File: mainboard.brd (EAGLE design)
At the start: 160 x 100 mm, 38 parts, among them IC1 LM358N, IC2 LM833N, IC3 74HC08N, K1 AQH213

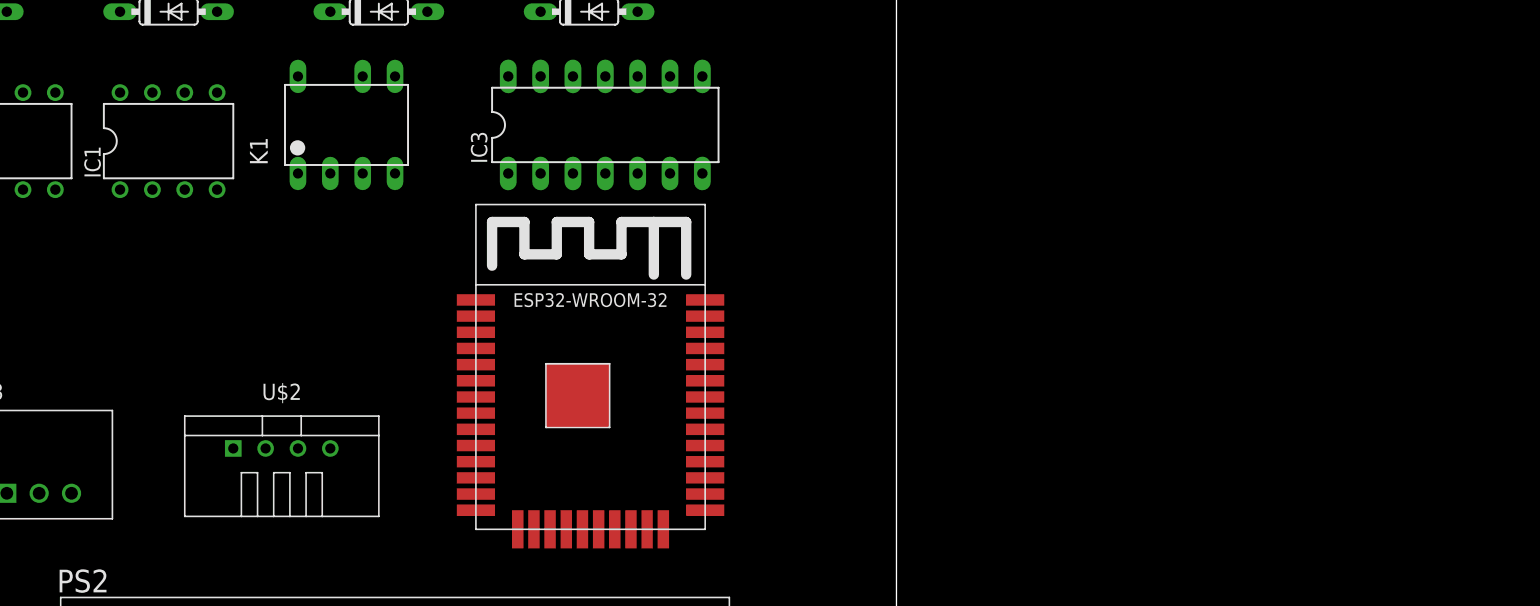
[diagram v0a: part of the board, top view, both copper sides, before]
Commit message: Added optos for sensing L and N (l1/l2)
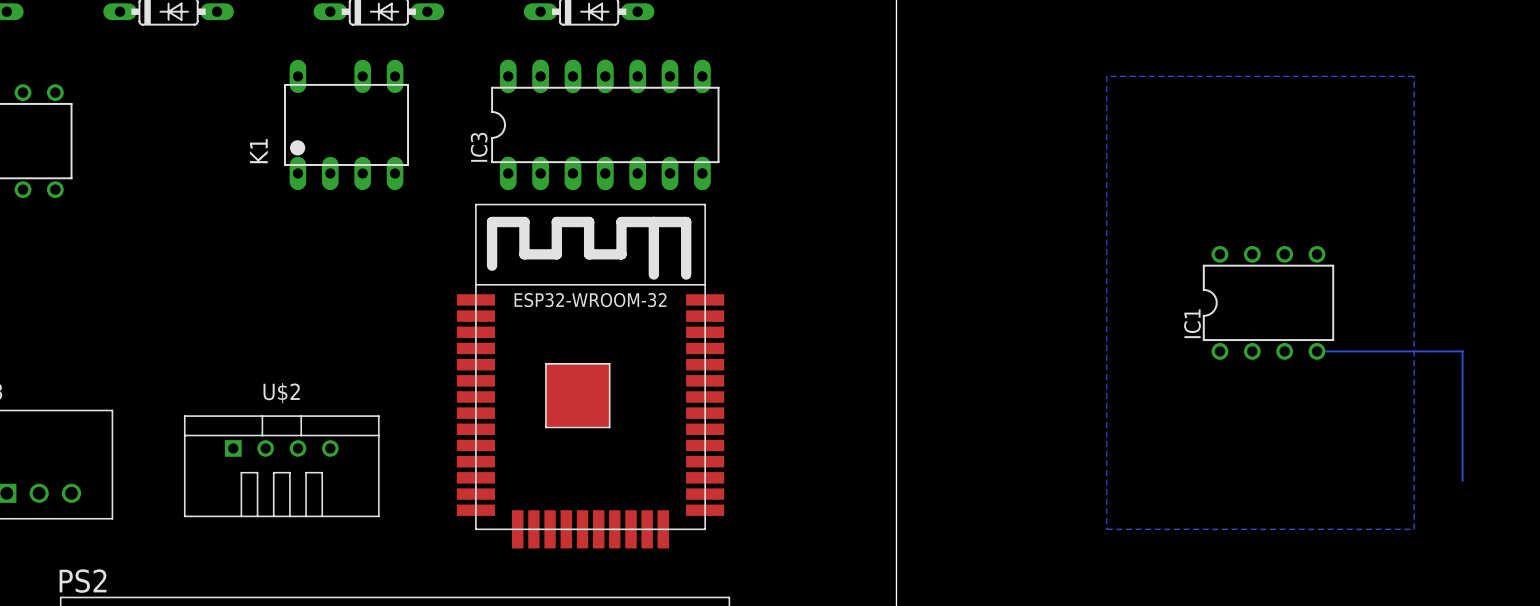
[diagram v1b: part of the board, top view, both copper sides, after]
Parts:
- moved IC1 87.3 mm to (29.2, 53.3)
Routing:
- net GND: track 0.00 -> 21.6 mm
- added copper zone on layer 16, net GND
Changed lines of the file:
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@@
 <?xml version="1.0" encoding="utf-8"?>
 <!DOCTYPE eagle SYSTEM "eagle.dtd">
-<eagle version="9.5.2">
+<eagle version="9.6.0">
 <drawing>
 <settings>
@@
 <attribute name="VALUE" x="-75.946" y="73.533" size="1.27" layer="27" ratio="10"/>
 </element>
-<element name="IC1" library="linear" library_urn="urn:adsk.eagle:library:262" package="DIL08" package3d_urn="urn:adsk.eagle:package:16409/2" value="LM358N" x="-57.15" y="66.04" smashed="yes">
-<attribute name="NAME" x="-62.484" y="63.119" size="1.27" layer="25" ratio="10" rot="R90"/>
-<attribute name="POPULARITY" value="7" x="0" y="0" size="1.778" layer="27" display="off"/>
-<attribute name="VALUE" x="-60.706" y="65.405" size="1.27" layer="27" ratio="10"/>
+<element name="IC1" library="linear" library_urn="urn:adsk.eagle:library:262" package="DIL08" package3d_urn="urn:adsk.eagle:package:16409/2" value="LM358N" x="29.21" y="53.34" smashed="yes">
+<attribute name="NAME" x="23.876" y="50.419" size="1.27" layer="25" ratio="10" rot="R90"/>
+<attribute name="POPULARITY" value="7" x="86.36" y="-12.7" size="1.778" layer="27" display="off"/>
+<attribute name="VALUE" x="25.654" y="52.705" size="1.27" layer="27" ratio="10"/>
 </element>
 <element name="IC2" library="linear" library_urn="urn:adsk.eagle:library:262" package="DIL08" package3d_urn="urn:adsk.eagle:package:16409/2" value="LM833N" x="-69.85" y="66.04" smashed="yes">
@@
 <contactref element="R16" pad="1"/>
 <contactref element="IC3" pad="7"/>
+<polygon width="0.1524" layer="16">
+<vertex x="16.51" y="71.12"/>
+<vertex x="16.51" y="35.56"/>
+<vertex x="40.64" y="35.56"/>
+<vertex x="40.64" y="71.12"/>
+</polygon>
+<wire x1="33.02" y1="49.53" x2="44.45" y2="49.53" width="0.1524" layer="16"/>
+<wire x1="44.45" y1="49.53" x2="44.45" y2="39.37" width="0.1524" layer="16"/>
 <wire x1="-19.05" y1="81.28" x2="-21.59" y2="96.52" width="0" layer="19" extent="1-1"/>
 <wire x1="-15.24" y1="63.5" x2="-19.05" y2="81.28" width="0" layer="19" extent="1-1"/>
@@
 <wire x1="-41.91" y1="63.5" x2="-39.37" y2="63.5" width="0" layer="19" extent="1-1"/>
 <wire x1="-46.99" y1="63.5" x2="-41.91" y2="63.5" width="0" layer="19" extent="1-1"/>
-<wire x1="-53.34" y1="62.23" x2="-46.99" y2="63.5" width="0" layer="19" extent="1-1"/>
 <wire x1="-44.45" y1="41.91" x2="-29.735" y2="35.56" width="0" layer="19" extent="1-1"/>
 <wire x1="-46.99" y1="41.91" x2="-44.45" y2="41.91" width="0" layer="19" extent="1-1"/>
-<wire x1="-54.61" y1="81.28" x2="-53.34" y2="62.23" width="0" layer="19" extent="1-1"/>
+<wire x1="-54.61" y1="81.28" x2="-46.99" y2="63.5" width="0" layer="19" extent="1-1"/>
 <wire x1="-60.96" y1="81.28" x2="-54.61" y2="81.28" width="0" layer="19" extent="1-1"/>
 <wire x1="-73.66" y1="86.36" x2="-60.96" y2="81.28" width="0" layer="19" extent="1-1"/>
@@
 <wire x1="-67.31" y1="38.39" x2="-46.99" y2="41.91" width="0" layer="19" extent="1-1"/>
 <wire x1="-16.51" y1="16.55" x2="-29.735" y2="35.56" width="0" layer="19" extent="1-1"/>
+<wire x1="33.02" y1="49.53" x2="-15.24" y2="63.5" width="0" layer="19" extent="1-1"/>
 </signal>
 <signal name="+3V3">
@@
 <contactref element="IC1" pad="8"/>
 <contactref element="R13" pad="2"/>
+<wire x1="-16.51" y1="26.71" x2="25.4" y2="57.15" width="0" layer="19" extent="1-1"/>
+<wire x1="-69.85" y1="38.39" x2="-16.51" y2="26.71" width="0" layer="19" extent="1-1"/>
 <wire x1="-73.66" y1="69.85" x2="-69.85" y2="38.39" width="0" layer="19" extent="1-1"/>
-<wire x1="-60.96" y1="69.85" x2="-73.66" y2="69.85" width="0" layer="19" extent="1-1"/>
-<wire x1="-57.15" y1="81.28" x2="-60.96" y2="69.85" width="0" layer="19" extent="1-1"/>
+<wire x1="-57.15" y1="81.28" x2="-73.66" y2="69.85" width="0" layer="19" extent="1-1"/>
 <wire x1="-74.93" y1="91.44" x2="-57.15" y2="81.28" width="0" layer="19" extent="1-1"/>
-<wire x1="-16.51" y1="26.71" x2="-69.85" y2="38.39" width="0" layer="19" extent="1-1"/>
 </signal>
 <signal name="-15V">
@@
 <contactref element="R11" pad="2"/>
 <contactref element="JP4" pad="2"/>
+<wire x1="-22.86" y1="86.36" x2="30.48" y2="49.53" width="0" layer="19" extent="1-1"/>
 <wire x1="-48.26" y1="81.28" x2="-22.86" y2="86.36" width="0" layer="19" extent="1-1"/>
 <wire x1="-54.61" y1="91.44" x2="-48.26" y2="81.28" width="0" layer="19" extent="1-1"/>
-<wire x1="-55.88" y1="62.23" x2="-48.26" y2="81.28" width="0" layer="19" extent="1-1"/>
 </signal>
 <signal name="N$9">
@@
 <contactref element="IC1" pad="1"/>
 <contactref element="D4" pad="A"/>
-<wire x1="-58.42" y1="62.23" x2="-36.83" y2="76.2" width="0" layer="19" extent="1-1"/>
-<wire x1="-60.96" y1="62.23" x2="-58.42" y2="62.23" width="0" layer="19" extent="1-1"/>
+<wire x1="25.4" y1="49.53" x2="27.94" y2="49.53" width="0" layer="19" extent="1-1"/>
+<wire x1="-36.83" y1="76.2" x2="25.4" y2="49.53" width="0" layer="19" extent="1-1"/>
 </signal>
 <signal name="N$10">
@@
 <contactref element="D6" pad="A"/>
 <contactref element="R15" pad="2"/>
-<wire x1="-58.42" y1="69.85" x2="-24.13" y2="96.52" width="0" layer="19" extent="1-1"/>
-<wire x1="-69.85" y1="76.2" x2="-58.42" y2="69.85" width="0" layer="19" extent="1-1"/>
+<wire x1="-24.13" y1="96.52" x2="27.94" y2="57.15" width="0" layer="19" extent="1-1"/>
+<wire x1="-69.85" y1="76.2" x2="-24.13" y2="96.52" width="0" layer="19" extent="1-1"/>
 </signal>
 <signal name="N$12">
@@
 <contactref element="D3" pad="C"/>
 <contactref element="R14" pad="2"/>
+<wire x1="-13.97" y1="96.52" x2="33.02" y2="57.15" width="0" layer="19" extent="1-1"/>
 <wire x1="-27.94" y1="76.2" x2="-13.97" y2="96.52" width="0" layer="19" extent="1-1"/>
-<wire x1="-53.34" y1="69.85" x2="-27.94" y2="76.2" width="0" layer="19" extent="1-1"/>
-<wire x1="-60.96" y1="76.2" x2="-53.34" y2="69.85" width="0" layer="19" extent="1-1"/>
+<wire x1="-60.96" y1="76.2" x2="-27.94" y2="76.2" width="0" layer="19" extent="1-1"/>
 </signal>
 <signal name="N$14">
@@
 <contactref element="R12" pad="2"/>
 <contactref element="R13" pad="1"/>
-<wire x1="-55.88" y1="69.85" x2="-44.45" y2="76.2" width="0" layer="19" extent="1-1"/>
-<wire x1="-64.77" y1="91.44" x2="-55.88" y2="69.85" width="0" layer="19" extent="1-1"/>
+<wire x1="-44.45" y1="76.2" x2="30.48" y2="57.15" width="0" layer="19" extent="1-1"/>
+<wire x1="-64.77" y1="91.44" x2="-44.45" y2="76.2" width="0" layer="19" extent="1-1"/>
 <wire x1="-82.55" y1="91.44" x2="-64.77" y2="91.44" width="0" layer="19" extent="1-1"/>
 </signal>
